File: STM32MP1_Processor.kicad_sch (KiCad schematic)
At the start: 6 parts, among them U1 STM32MP131DAFx

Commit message: added mmc schematic
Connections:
- net EMMC5: now reaches U1.A15 (PB9)
- net EMMC4: now reaches U1.A16 (PF0)
- net EMMC6: now reaches U1.B14 (PC6)
- net EMMC1: now reaches U1.B15 (PB15)
- net EMMC0: now reaches U1.B16 (PB14)
- net EMMC9: now reaches U1.B17 (PE3)
- net EMMC7: now reaches U1.C13 (PC7)
- net EMMC2: now reaches U1.C14 (PB3)
- net EMMC3: now reaches U1.C16 (PB4)
- net EMMC8: now reaches U1.C17 (PG6)
- net EMMC10: now reaches U1.Y11 (NRST)

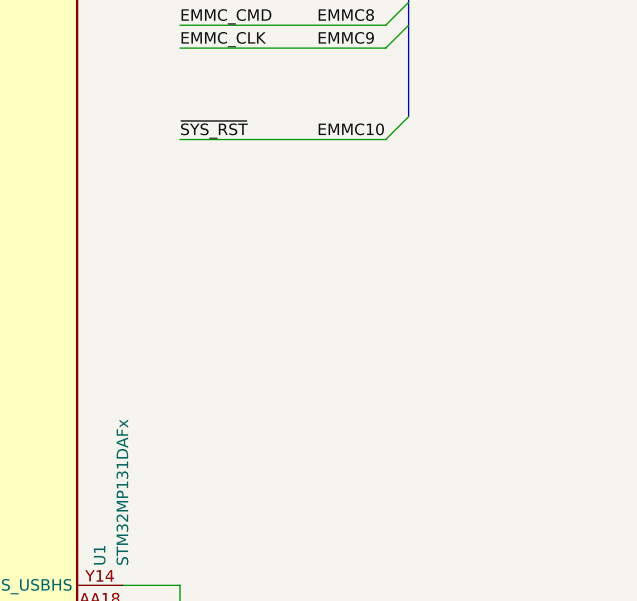
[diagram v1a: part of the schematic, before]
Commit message: Included Tushar's changed also added SDCARD module
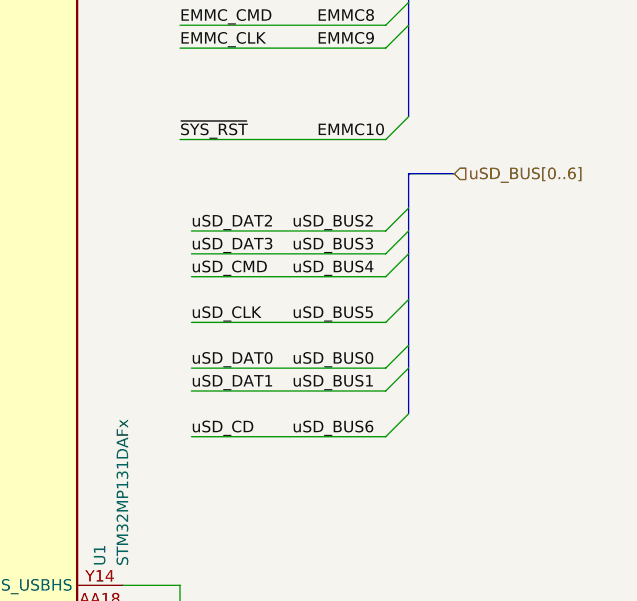
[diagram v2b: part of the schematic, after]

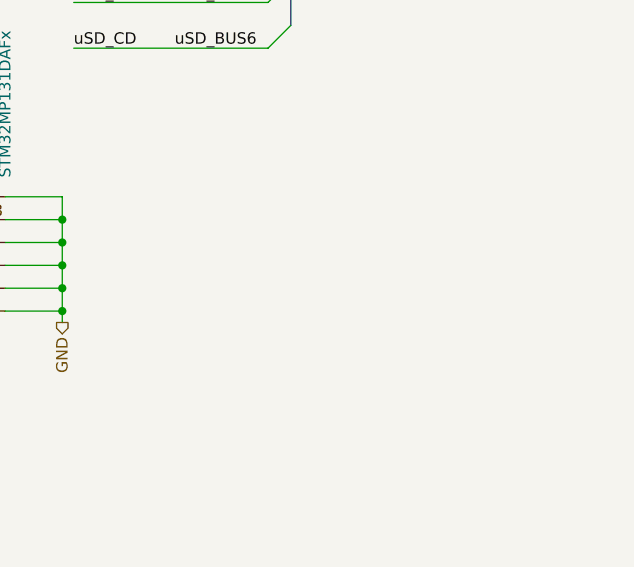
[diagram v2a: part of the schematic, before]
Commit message: Completed ETH Module as per ref schematic also populated compatible busses in processor module
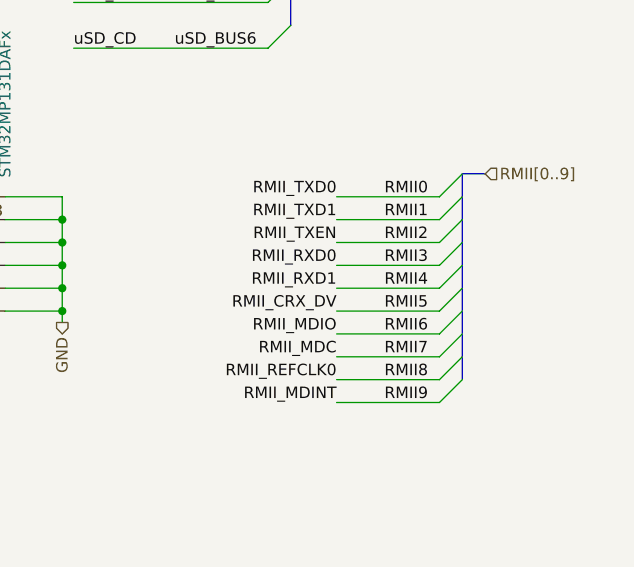
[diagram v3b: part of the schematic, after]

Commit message: Updated Processor With ETH Pins
Also updated Capacitors and Resistors to 402
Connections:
- net RMII0: now also U1.AA9 (PG13)
- net RMII1: now also U1.Y10 (PG14)
- net RMII2: now also U1.AA2 (PB11)
- net RMII3: now also U1.Y7 (PC4)
- net RMII4: now also U1.AA7 (PC5)
- net RMII6: now also U1.Y4 (PA2)
- net RMII7: now also U1.V3 (PG2)
- net RMII_REFCLK: now reaches U1.AA3 (PA1)
- net RMII_NRST: now reaches U1.W1 (PG3)
- net RMII_CRS_DV: now reaches U1.Y9 (PC1)

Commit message: Added PMIC, WIFI and updated to STM32MP157 design
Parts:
- removed U1: STM32MP131DAFx, Package_BGA:ST_TFBGA-320_11x11mm_Layout21x21_P0.5mm, symbol MCU_ST_STM32MP1:STM32MP131DAFx
- added C67, C68, C69, C70, C71, C72, C73, C74, C75, C76, C77, C78, C79, C80, C81, C82, C89, C90: 1uF, Capacitor_SMD:C_0402_1005Metric, symbol Device:C_Small
- added C83, C84: 1nF, Capacitor_SMD:C_0402_1005Metric, symbol Device:C_Small
- added C85, C87, C91: 2.2uF, Capacitor_SMD:C_0402_1005Metric, symbol Device:C_Small
- added C86, C88, C92: 100nF, Capacitor_SMD:C_0402_1005Metric, symbol Device:C_Small
- added L2: 4.7uH, symbol Device:L
- added R103: 0R, Resistor_SMD:R_0402_1005Metric, symbol Device:R_Small
- added U7: STM32MP157DACx, Package_BGA:ST_TFBGA-361_12x12mm_Layout23x23_P0.5mmP0.65mm, symbol MCU_ST_STM32MP1:STM32MP157DACx
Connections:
- net GND: now also C67.1, C68.1, C69.1, C70.1, C71.1, C72.1, C73.1, C74.1, C75.1, C76.1, C77.1, C78.1, C79.1, C80.1, C81.1, C82.1, C83.1, C84.1, C85.2, C86.2, C87.2, C88.2, C89.2, C90.2, C91.2, C92.2, U7.1A3 (VSS), U7.1A5 (VSS), U7.1A7 (VSS), U7.1B2 (VSS), U7.1B4 (VSS), U7.1B6 (VSS), U7.1B8 (VSS), U7.1C1 (VSS), U7.1C3 (VSS), U7.1C5 (VSS), U7.1C7 (VSS), U7.1C9 (VSS), U7.1D2 (VSS), U7.1D4 (VSS), U7.1D6 (VSS), U7.1D8 (VSS), U7.1E1 (VSS), U7.1E3 (VSS), U7.1E5 (VSS), U7.1E7 (VSS), U7.1E9 (VSS), U7.1F2 (VSS), U7.1F4 (VSS), U7.1F6 (VSS), U7.1F8 (VSS), U7.1G1 (VSS_ANA), U7.1G3 (VSS), U7.1G5 (VSS), U7.1G7 (VSS), U7.1G9 (VSS), U7.1H2 (VSSA), U7.1H4 (VSS), U7.1H6 (VSS), U7.1H8 (VSS), U7.1J3 (VSS), U7.1J5 (VSS), U7.1J7 (VSS), U7.A1 (VSS), U7.A23 (VSS), U7.AA12 (VSS), U7.AA16 (VSS_USBHS), U7.AA21 (VSS), U7.AA5 (VSS), U7.AA8 (VSS), U7.AC1 (VSS), U7.AC23 (VSS), U7.C12 (VSS), U7.C16 (VSS_DSI), U7.C21 (VSS), U7.C7 (VSS), U7.D4 (VSS), U7.F21 (VSS), U7.H3 (VSS), U7.K21 (VSS), U7.P21 (VSS), U7.P3 (VSS), U7.V21 (VSS), U7.W3 (VSS)
- net VDD_CORE: now also C67.2, C68.2, C69.2, C70.2, C71.2, C72.2, C73.2, C74.2, U7.1A2 (VDDCORE), U7.1A4 (VDDCORE), U7.1A6 (VDDCORE), U7.1B1 (VDDCORE), U7.1B3 (VDDCORE), U7.1B5 (VDDCORE), U7.1C2 (VDDCORE), U7.1C4 (VDDCORE), U7.1C6 (VDDCORE), U7.1D1 (VDDCORE), U7.1D3 (VDDCORE), U7.1D5 (VDDCORE), U7.1D7 (VDDCORE), U7.1E2 (VDDCORE), U7.1E4 (VDDCORE), U7.1E6 (VDDCORE), U7.1F5 (VDDCORE), U7.1F7 (VDDCORE), U7.1G6 (VDDCORE), U7.1H7 (VDDCORE)
- net VDD_DDR: now also C81.2, C82.2, C83.2, C84.2, U7.1A8 (VDDQ_DDR), U7.1B7 (VDDQ_DDR), U7.1B9 (VDDQ_DDR), U7.1C8 (VDDQ_DDR), U7.1D9 (VDDQ_DDR), U7.1E8 (VDDQ_DDR), U7.1F9 (VDDQ_DDR), U7.1G2 (VDD_ANA), U7.1G8 (VDDQ_DDR), U7.1H9 (VDDQ_DDR), U7.1J8 (VDDQ_DDR), U7.B18 (VDD_DSI)
- new net: L2.1, R103.1
- new net: C89.1, L2.2, U7.1H1 (VDDA)
- new net: C88.1, U7.AA15 (VDD3V3_USBHS), U7.AA17 (VDD3V3_USBFS)
- new net: C87.1, U7.AB15 (VDDA1V1_REG)
- new net: C91.1, U7.C17 (VDD1V2_DSI_PHY), U7.C18 (VDD1V2_DSI_REG)
- new net VBAT: C92.1, U7.1F1 (VBAT)
- new net VDD: C75.2, C76.2, C77.2, C78.2, C79.2, C80.2, R103.2, U7.1F3 (VDD), U7.1G4 (VDD), U7.1H3 (VDD), U7.1H5 (VDD), U7.1J2 (VDD), U7.1J4 (VDD), U7.1J6 (VDD)
- new net VDDA_1V8: C85.1, C86.1, U7.AB14 (VDDA1V8_REG), U7.C14 (VDDA1V8_DSI)
- new net VREF+: C90.1, U7.R4 (VREF+)
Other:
- moved on the sheet: C3, R5, TP_1, TP_2, TP_3
